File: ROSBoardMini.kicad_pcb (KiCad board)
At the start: 4 copper layers, 65 x 30 mm, 75 parts, among them J1 Conn_02x20_Odd_Even, J2 Extension0, J3 Extension1, J4 Extension2, J5 PWR, J6 Extension2, U1 P2X8C4M64P, U10 LY68L6400SLIT, U2 W25Q128JVS, U3 PCA9544APW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

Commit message: Rooting progress
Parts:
- removed D1: D, Diode_SMD:D_0805_2012Metric
- C13, C25, C26, C27, C28, C29, C30, J3, R10, U7, U8, U9: moved to B.Cu
- J6, U10, U2: moved to F.Cu
- moved C31 130.3 mm to (98.3, 57.1), turned to 270 degrees
- moved C1 104.1 mm to (63.8, 68.6), turned to 90 degrees
- moved D2 70.8 mm to (55.4, 64.3), turned to 270 degrees
- moved D3 68.0 mm to (55.6, 67.8), turned to 180 degrees
- moved C9 49.6 mm to (112.5, 61.7), turned to 270 degrees
- moved C8 45.0 mm to (112.5, 59.7), turned to 90 degrees
- moved C13 42.8 mm to (103.4, 58.2), turned to 270 degrees
- moved R7 41.7 mm to (70.1, 30.0)
- moved C14 39.9 mm to (133.5, -1.17)
- moved C15 39.9 mm to (124.5, 2.89)
- moved C16 39.9 mm to (124.5, 4.88)
- moved C17 39.9 mm to (127.4, 2.89)
- moved C18 39.9 mm to (130.6, -1.17)
- moved C19 39.9 mm to (133.5, -3.16)
- moved C20 39.9 mm to (124.5, 6.87)
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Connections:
- J5 pad 1: Net-(D1-Pad2) -> +BATT
- J6 pad 1: /GPIO26 -> /IO0
- J6 pad 16: /IO0 -> /GPIO26
- J6 pad 17: /IO1 -> /GPIO23
- J6 pad 18: /IO2 -> /GPIO24
- J6 pad 19: /IO3 -> /GPIO28
- J6 pad 2: /GPIO23 -> /IO1
- J6 pad 20: /IO4 -> /GPIO29
- J6 pad 3: /GPIO24 -> /IO2
- J6 pad 4: /GPIO29 -> /IO3
- J6 pad 5: /GPIO28 -> /IO4
- J6 pad 6: /GPIO1 -> /GPIO8
- J6 pad 8: /GPIO8 -> /GPIO1
- U1 pad 10: /SPI_MOSI -> /CSI2_MCLK
- U1 pad 12: /SPI_MISO -> /CSI2_HSYNC
- U1 pad 13: /SPI_SCK -> /CSI2_VSYNC
- U1 pad 15: /CSI1_D0 -> /CSI1_PCLK
- U1 pad 16: /CSI1_D1 -> /CSI1_MCLK
- U1 pad 18: /CSI1_D2 -> /CSI1_HSYNC
- U1 pad 19: /CSI1_D3 -> /CSI1_VSYNC
- U1 pad 21: /CSI1_D4 -> /I2C_SDA
- U1 pad 22: /CSI1_D5 -> /I2C_SCL
- U1 pad 24: /CSI1_D6 -> /IO0
- U1 pad 25: /CSI1_D7 -> /IO1
- U1 pad 27: /CSI2_D0 -> /IO2
- U1 pad 28: /CSI2_D1 -> /IO3
- U1 pad 3: Net-(U1-Pad3) -> /CSI0_VSYNC
- U1 pad 30: /CSI2_D2 -> /IO4
- U1 pad 31: /CSI2_D3 -> /IO5
- U1 pad 33: /CSI2_D4 -> Net-(U1-Pad33)
- U1 pad 34: /CSI2_D5 -> Net-(U1-Pad34)
- U1 pad 36: /CSI2_D6 -> Net-(U1-Pad36)
- U1 pad 37: /CSI2_D7 -> Net-(U1-Pad37)
- U1 pad 39: /CSI0_MCLK -> Net-(U1-Pad39)
- U1 pad 4: Net-(U1-Pad4) -> /CSI0_HSYNC
- U1 pad 40: /CSI1_MCLK -> /PSRAM_SCLK
- U1 pad 42: /CSI2_MCLK -> /PSRAM_CE
- U1 pad 43: /CSI0_PCLK -> /PSRAM_D3
- U1 pad 45: /CSI1_PCLK -> /PSRAM_D2
- U1 pad 46: /CSI2_PCLK -> /PSRAM_D1
- U1 pad 48: /CSI0_HSYNC -> /PSRAM_D0
- U1 pad 49: /CSI1_HSYNC -> /SPI_SCK
- U1 pad 53: /CSI2_HSYNC -> /SPI_MOSI
- U1 pad 54: /CSI0_VSYNC -> /SPI_MISO
- U1 pad 56: /CSI1_VSYNC -> /CSI1_D0
- U1 pad 57: /CSI2_VSYNC -> /CSI1_D1
- U1 pad 59: /CSI_RST -> /CSI1_D2
- U1 pad 6: Net-(U1-Pad6) -> /CSI0_MCLK
- U1 pad 60: /CSI_PWDN -> /CSI1_D3
- U1 pad 62: Net-(U1-Pad62) -> /CSI1_D4
- U1 pad 63: /I2C_SCL -> /CSI1_D5
- U1 pad 65: /I2C_SDA -> /CSI1_D6
- U1 pad 66: /CSI0_D7 -> /CSI1_D7
- U1 pad 68: /CSI0_D6 -> /CSI2_D0
- U1 pad 69: /CSI0_D5 -> /CSI2_D1
- U1 pad 7: +BATT -> /CSI0_PCLK
- U1 pad 71: /CSI0_D4 -> /CSI2_D2
- U1 pad 72: /CSI0_D3 -> /CSI2_D3
- U1 pad 74: /CSI0_D2 -> /CSI2_D4
- U1 pad 75: /CSI0_D1 -> /CSI2_D5
- U1 pad 77: /CSI0_D0 -> /CSI2_D6
- U1 pad 78: /PSRAM_D3 -> /CSI2_D7
- U1 pad 80: /PSRAM_CE -> /CSI0_D0
- U1 pad 81: /PSRAM_SCLK -> /CSI0_D1
- U1 pad 83: /IO0 -> /CSI0_D2
- U1 pad 84: /IO1 -> /CSI0_D3
- U1 pad 86: /IO2 -> /CSI0_D4
- U1 pad 87: /IO3 -> /CSI0_D5
- U1 pad 89: /IO4 -> /CSI0_D6
- U1 pad 9: /SPI_CS0 -> /CSI2_PCLK
- U1 pad 90: /IO5 -> /CSI0_D7
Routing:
- net /GPIO8: track 0.00 -> 47.5 mm, vias 0 -> 1
- net /GPIO9: track 0.00 -> 44.2 mm, vias 0 -> 1
- net /GPIO1: track 0.00 -> 38.8 mm, vias 0 -> 1
- net /CSI1_D1: track 0.00 -> 32.6 mm, vias 0 -> 2
- net /GPIO26: track 0.00 -> 28.8 mm, vias 0 -> 1
- net /CSI1_D2: track 0.00 -> 28.7 mm, vias 0 -> 1
- net /GPIO29: track 0.00 -> 28.3 mm, vias 0 -> 1
- net /CSI2_VSYNC: track 0.00 -> 27.8 mm, vias 0 -> 1
- net /CSI1_D3: track 0.00 -> 27.7 mm, vias 0 -> 1
- net /CSI1_D0: track 0.00 -> 27.5 mm, vias 0 -> 2
- net /PSRAM_SCLK: track 0.00 -> 27.3 mm
- net /CSI1_D4: track 0.00 -> 27.3 mm, vias 0 -> 1
- net /GPIO24: track 0.00 -> 27.1 mm, vias 0 -> 1
- net /CSI1_D6: track 0.00 -> 27.1 mm, vias 0 -> 1
- net /CSI1_D7: track 0.00 -> 27.0 mm, vias 0 -> 1
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- added copper zone on In1.Cu, net GND
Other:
- net class Power: clearance 0.4 -> 0.15

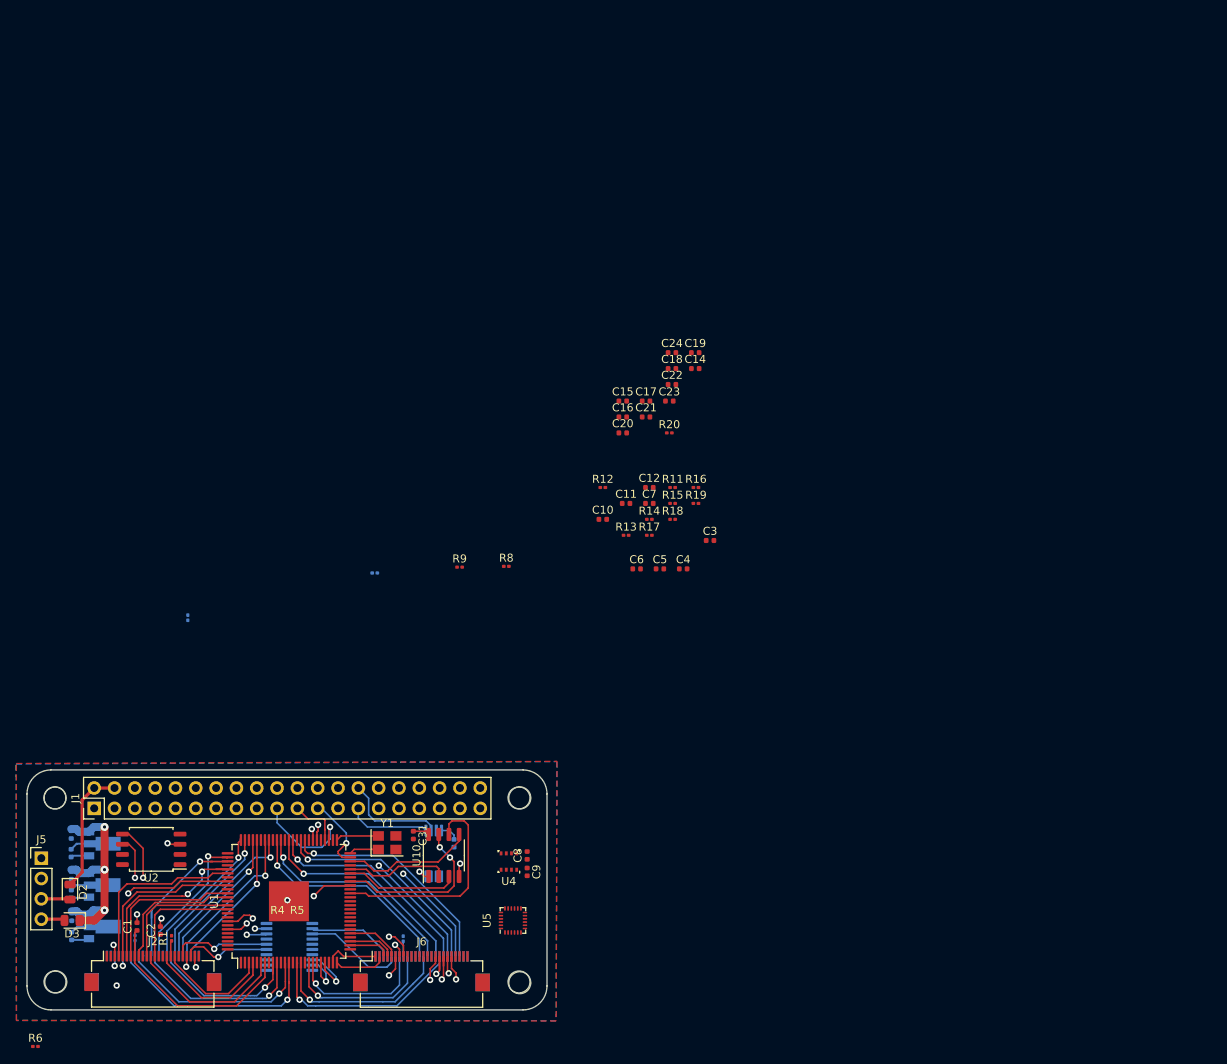
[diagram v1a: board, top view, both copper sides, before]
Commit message: Re arrange pin to allow 1 cog to use 3 camera + rooting progress
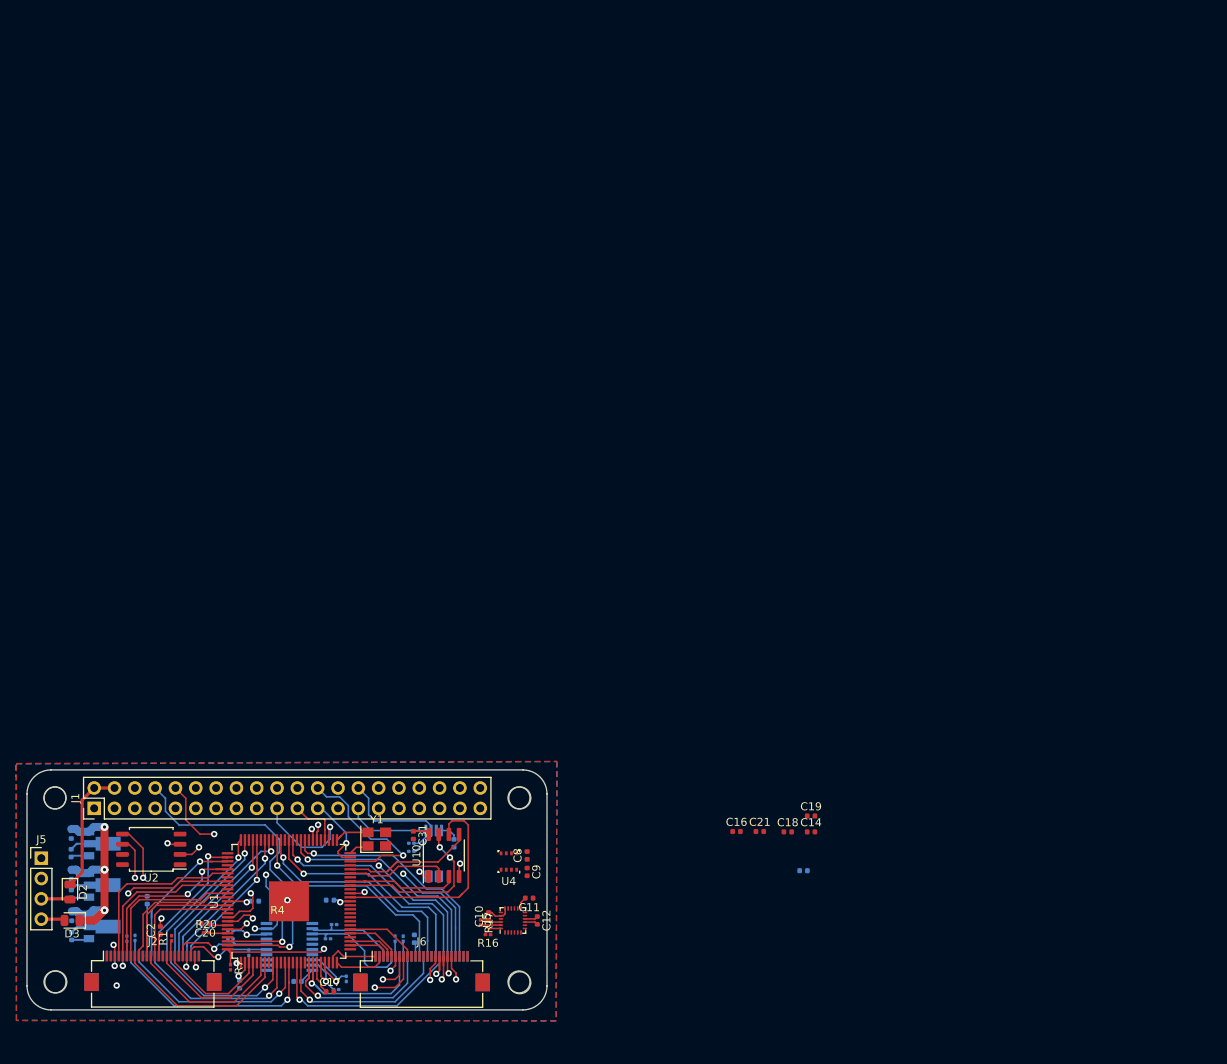
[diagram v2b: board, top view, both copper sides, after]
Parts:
- removed C1, C3, C5: 15pF, Capacitor_SMD:C_0402_1005Metric
- C15, C22, C23, C24, C4, C6, C7, R11, R12, R13, R14, R15, R18, R19, R5, R6, R8, R9: moved to B.Cu
- R7: moved to F.Cu
- moved C22 92.4 mm to (76.6, 75.8), turned to 270 degrees
- moved C24 86.1 mm to (78.5, 65.4)
- moved R20 85.2 mm to (72.4, 69.3)
- moved C17 83.7 mm to (87.9, 76.7)
- moved C20 80.5 mm to (72.3, 68.2), turned to 180 degrees
- moved R11 79.0 mm to (75.4, 70.1)
- moved C7 74.2 mm to (83.8, 75.4), turned to 180 degrees
- moved C6 73.9 mm to (65.0, 65.3), turned to 90 degrees
- moved R19 73.8 mm to (89.9, 75.1), turned to 90 degrees
- moved R14 73.4 mm to (75.4, 69.1)
- moved C15 72.3 mm to (87.9, 65.3), turned to 180 degrees
- moved R18 72.3 mm to (88.6, 76.5), turned to 180 degrees
- moved R15 71.1 mm to (81.3, 66.8), turned to 270 degrees
- moved R12 64.1 mm to (88.4, 68.3), turned to 180 degrees
- moved R13 62.7 mm to (87.6, 70.1), turned to 180 degrees
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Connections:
- J6 pad 11: /SPI_MISO -> /SPI_MOSI
- J6 pad 12: /SPI_SCK -> /SPI_MISO
- J6 pad 13: /SPI_CS1 -> /SPI_SCK
- J6 pad 22: /IO5 -> /SPI_CS1
- J6 pad 6: /GPIO8 -> /GPIO1
- J6 pad 8: /GPIO1 -> /GPIO8
- J6 pad 9: /SPI_MOSI -> /IO5
- U1 pad 33: Net-(U1-Pad33) -> /CSI_RST
- U1 pad 34: Net-(U1-Pad34) -> /CSI_PWDN
- U1 pad 36: Net-(U1-Pad36) -> +BATT
- U1 pad 39: Net-(U1-Pad39) -> /PSRAM_SCLK
- U1 pad 40: /PSRAM_SCLK -> /PSRAM_CE
- U1 pad 42: /PSRAM_CE -> /PSRAM_D3
- U1 pad 43: /PSRAM_D3 -> /PSRAM_D2
- U1 pad 45: /PSRAM_D2 -> /PSRAM_D1
- U1 pad 46: /PSRAM_D1 -> /PSRAM_D0
- U1 pad 48: /PSRAM_D0 -> /SPI_CS0
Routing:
- net /P2_RX: track 0.00 -> 42.2 mm, vias 0 -> 1
- net /P2_RST: track 0.00 -> 35.5 mm, vias 0 -> 1
- net /P2_TX: track 0.00 -> 34.0 mm, vias 0 -> 3
- net /SPI_CS0: track 0.00 -> 21.9 mm, vias 0 -> 1
- net /P58: track 0.00 -> 17.3 mm, vias 0 -> 2
- net +1V8: track 2.53 -> 19.5 mm, vias 0 -> 3
- net +3V3: track 33.6 -> 48.2 mm
- net /PSRAM_CE: track 21.1 -> 12.1 mm
- net /IO5: track 0.00 -> 9.06 mm
- net GND: track 12.0 -> 16.2 mm
- net /CSI1_VSYNC: track 18.6 -> 22.6 mm
- net /EEPROM_SCL: track 12.8 -> 16.5 mm
- net /CSI0_PCLK: track 26.0 -> 22.7 mm
- net /GPIO9: track 44.2 -> 47.4 mm
- net /GPIO8: track 47.5 -> 50.5 mm
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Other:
- net class Power removed

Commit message: Everything rooted except power
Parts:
- removed R1, R2, R3, R4, R5, R6: 1K, Resistor_SMD:R_0201_0603Metric
- C14: moved to B.Cu
- C23: moved to F.Cu
- moved C18 83.5 mm to (61.8, 62.5), turned to 180 degrees
- moved C19 79.1 mm to (70.4, 69.9), turned to 180 degrees
- moved C21 73.1 mm to (69.3, 67.0), turned to 180 degrees
- moved C23 63.9 mm to (83.4, 56.2), turned to 180 degrees
- moved C14 60.0 mm to (88.0, 57.7)
- moved C16 47.3 mm to (92.4, 66.2), turned to 90 degrees
- moved R13 3.68 mm to (91.3, 69.6)
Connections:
- J2 pad 17: Net-(J2-Pad17) -> /CSI_PWDN
- J2 pad 19: Net-(J2-Pad19) -> /CSI_RST
- J3 pad 17: Net-(J3-Pad17) -> /CSI_PWDN
- J3 pad 19: Net-(J3-Pad19) -> /CSI_RST
- J4 pad 17: Net-(J4-Pad17) -> /CSI_PWDN
- J4 pad 19: Net-(J4-Pad19) -> /CSI_RST
- J6 pad 11: /SPI_MOSI -> /SPI_MISO
- J6 pad 12: /SPI_MISO -> /SPI_MOSI
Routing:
- net +3V3: track 48.2 -> 106.2 mm, vias 4 -> 12
- net /CSI_PWDN: track 0.00 -> 55.1 mm, vias 0 -> 3
- net /CSI_RST: track 0.00 -> 54.1 mm, vias 0 -> 3
- net +BATT: track 0.00 -> 41.3 mm, vias 0 -> 1
- net /SPI_CS1: track 0.00 -> 37.9 mm
- net /I2C_SDA: track 7.20 -> 42.7 mm, vias 1 -> 2
- net /I2C_SCL: track 8.89 -> 42.3 mm, vias 1 -> 2
- net /SPI_MISO: track 6.55 -> 35.8 mm, vias 0 -> 2
- net /I2C3_SDA: track 2.37 -> 27.9 mm, vias 0 -> 2
- net /I2C3_SCL: track 2.57 -> 27.8 mm, vias 0 -> 2
- net /SPI_MOSI: track 13.3 -> 36.1 mm, vias 1 -> 3
- net /SPI_SCK: track 9.53 -> 31.9 mm, vias 1 -> 3
- net +1V2: track 2.61 -> 9.69 mm, vias 0 -> 3
- net GND: track 16.2 -> 23.3 mm, vias 6 -> 8
- net +1V8: track 19.5 -> 25.2 mm, vias 3 -> 6
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
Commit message: Rooting done
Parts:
- removed C16, C21: 4.7uF, Capacitor_SMD:C_0402_1005Metric
- moved C23 8.37 mm to (75.0, 56.4)
- moved R14 2.95 mm to (78.2, 70.2)
- moved R12 1.98 mm to (90.3, 68.9), turned to 0 degrees
- moved R10 1.77 mm to (76.0, 71.9), turned to 0 degrees
- moved C22 1.61 mm to (77.9, 74.8), turned to 0 degrees
- moved R18 1.16 mm to (89.8, 76.4)
- moved R11 1.05 mm to (75.9, 71.0)
- moved R13 1.00 mm to (90.3, 69.8), turned to 0 degrees
- moved C2 0.74 mm to (67.1, 68.4), turned to 0 degrees
- moved R19 0.45 mm to (89.8, 75.6), turned to 180 degrees
- moved C15 0.42 mm to (87.6, 65.5)
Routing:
- net +3V3: track 106.2 -> 331.4 mm, vias 12 -> 28
- net +1V8: track 25.2 -> 182.3 mm, vias 6 -> 18
- net GND: track 23.3 -> 95.5 mm, vias 8 -> 26
- net +1V2: track 9.69 -> 75.3 mm, vias 3 -> 5
- net +2V8: track 3.89 -> 58.7 mm, vias 1 -> 3
- net /GPIO24: track 27.1 -> 33.4 mm
- net /SPI_MISO: track 35.8 -> 40.5 mm
- net /CSI1_D0: track 29.1 -> 32.1 mm
- net /CSI2_D7: track 19.1 -> 21.9 mm
- net /SPI_MOSI: track 36.1 -> 38.0 mm
- net /I2C3_SCL: track 27.8 -> 29.6 mm, vias 2 -> 3
- net /CSI1_D7: track 28.3 -> 29.9 mm
- net /GPIO26: track 28.8 -> 30.4 mm
- net /SPI_SCK: track 31.9 -> 33.5 mm
- net /CSI1_PCLK: track 25.7 -> 27.2 mm
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- added copper zone on In2.Cu, net GND

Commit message: Clean schematic and rename 4th connector
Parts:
- J6: value Extension2 -> Extension3

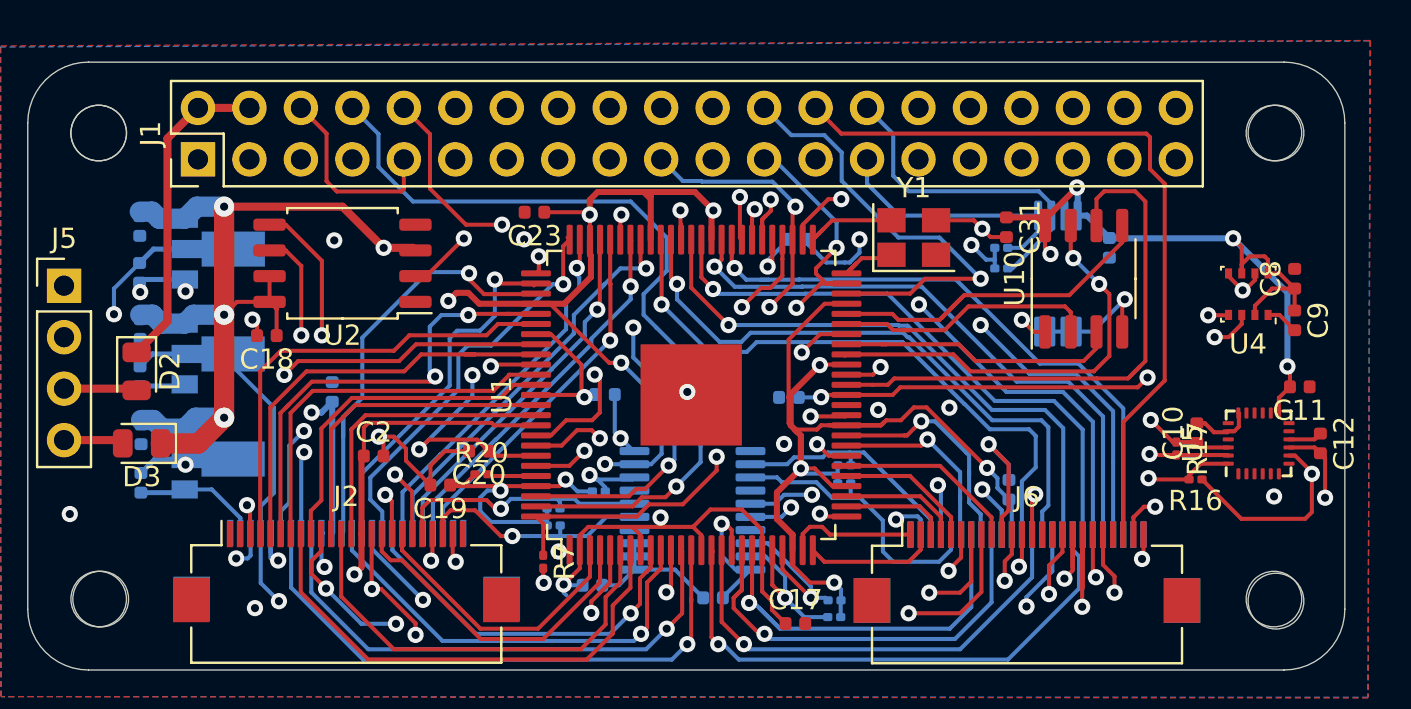
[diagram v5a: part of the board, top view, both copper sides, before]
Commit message: Various cleaning, doc in schematic and replaced problematic 2.8V ldo
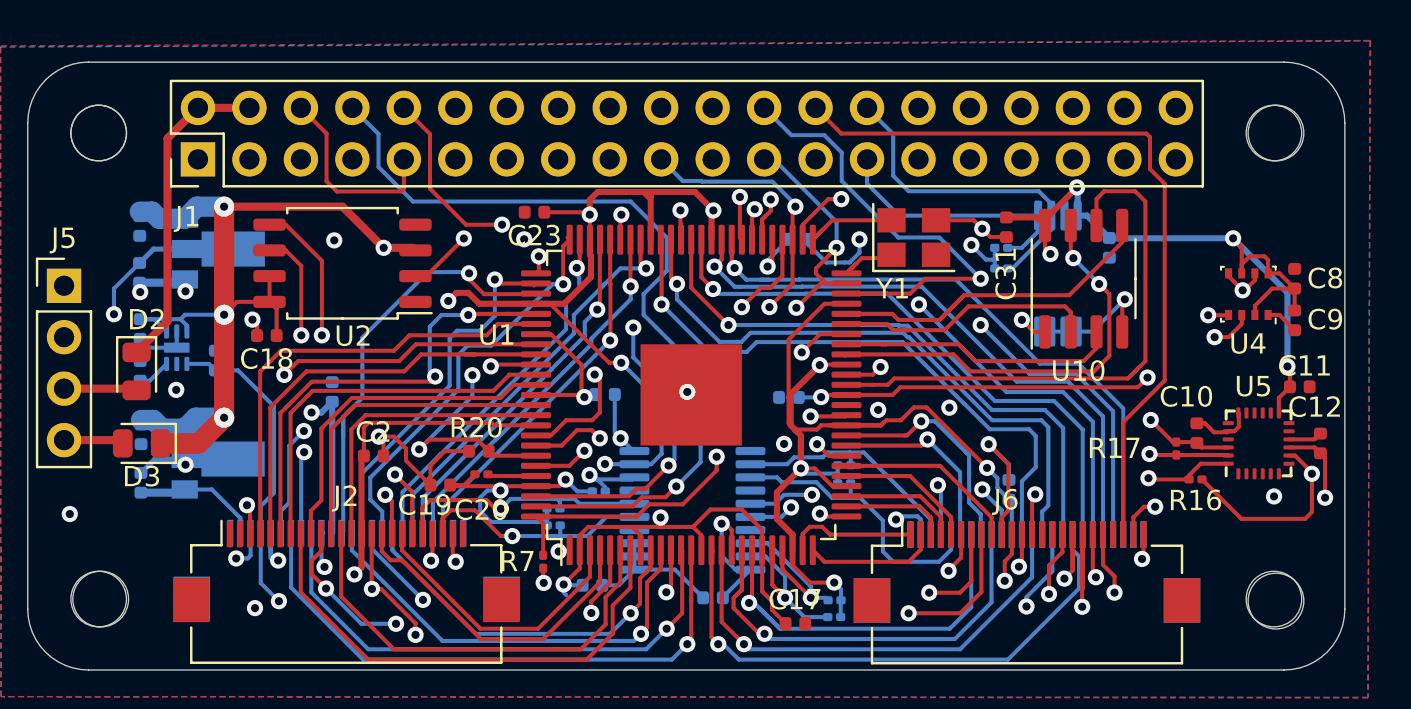
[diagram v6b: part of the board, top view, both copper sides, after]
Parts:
- added C1: 0.1uF, Capacitor_SMD:C_0402_1005Metric, B.Cu at (55.5, 64.2)
- C13, C18, C31, C7, C8, C9: value 100nF -> 0.1uF
- C27: value 10uF -> 1uF
- C30: value 22uF -> 1uF
- U9: value AZ1117-2.85 -> MIC5353-2.8YMT; footprint Package_TO_SOT_SMD:SOT-89-3 -> Package_DFN_QFN:MLF-6-1EP_1.6x1.6mm_P0.5mm_EP0.5x1.26mm
- moved C30 3.80 mm to (59.3, 63.7), turned to 90 degrees
- moved U9 2.07 mm to (57.4, 63.1), turned to 270 degrees
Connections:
- U9 pad 1: GND -> +3V3
- U9 pad 2: +2V8 -> GND
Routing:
- net +2V8: track 58.7 -> 56.0 mm
- net +3V3: track 331.4 -> 333.4 mm
- net Net-(C1-Pad1): track 0.00 -> 1.65 mm
- net GND: track 95.5 -> 96.0 mm, vias 26 -> 27
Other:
- board text added: "ROS Board Mini V1.0"
